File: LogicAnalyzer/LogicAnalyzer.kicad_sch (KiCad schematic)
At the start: 29 parts, among them J1 Conn_02x03_Odd_Even, J2 Connector, J3 Chain, U1 TXB0104PW, U2 TXB0104PW, U3 TXB0104PW, U4 TXB0104PW, U5 TXB0104PW, U6 TXB0104PW, U7 Pico

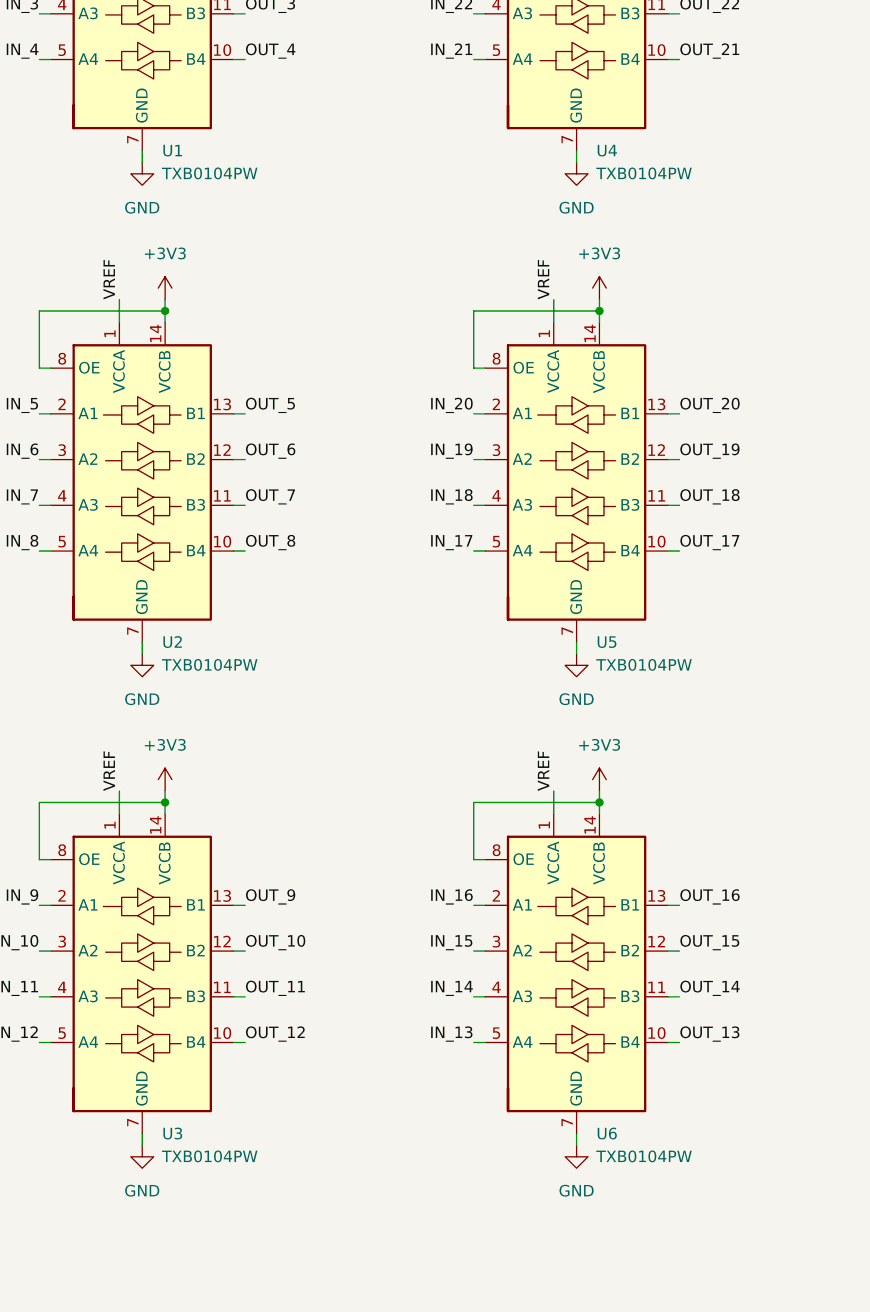
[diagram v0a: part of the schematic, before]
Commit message: Schematic Update Level Shifter Type
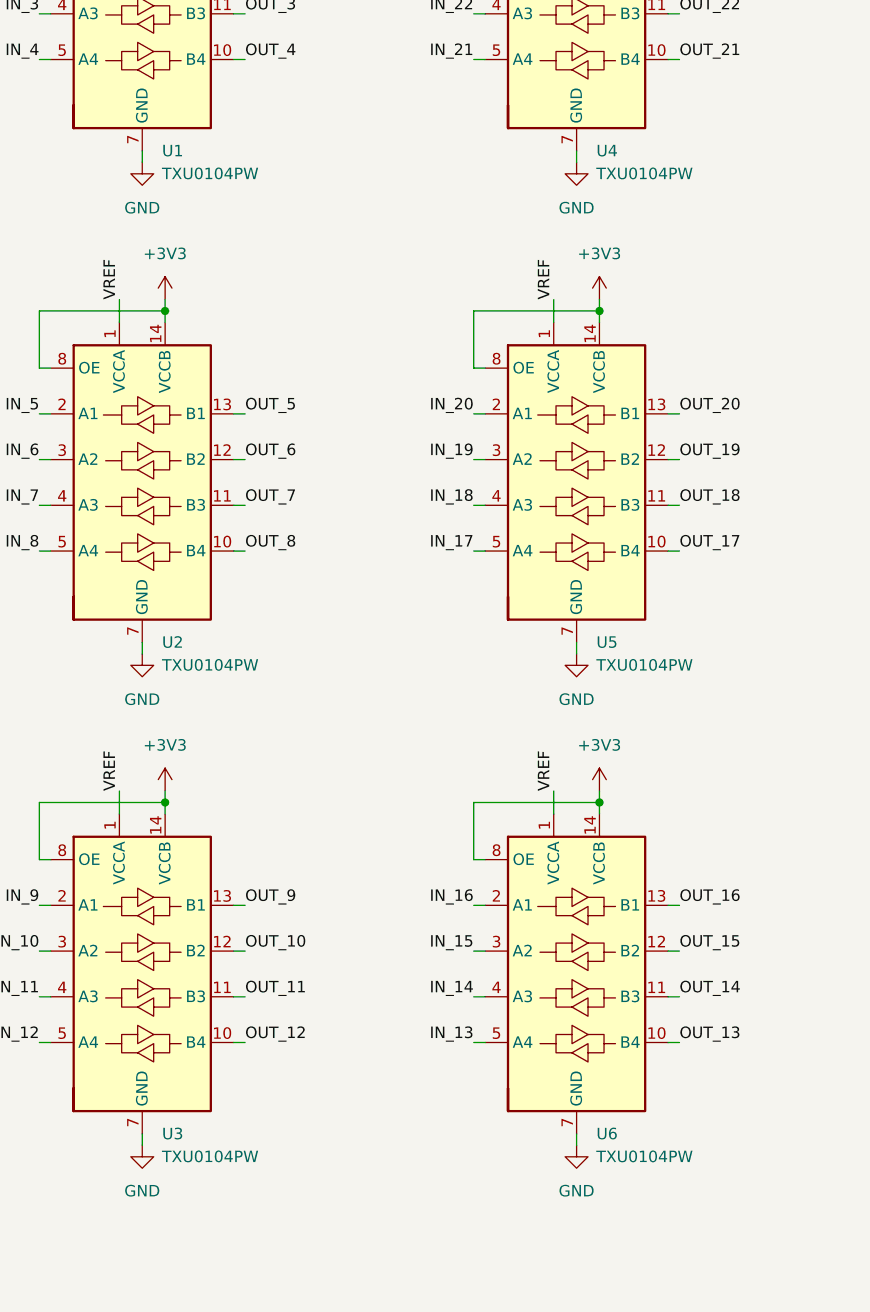
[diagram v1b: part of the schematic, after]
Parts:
- U1, U2, U3, U4, U5, U6: value TXB0104PW -> TXU0104PW
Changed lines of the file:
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@@
 			)
 		)
-		(property "Value" "TXB0104PW"
+		(property "Value" "TXU0104PW"
 			(at 41.5641 181.61 0)
 			(effects
@@
 			)
 		)
-		(property "Datasheet" "http://www.ti.com/lit/ds/symlink/txb0104.pdf"
+		(property "Datasheet" "https://www.ti.com/lit/ds/symlink/txu0104.pdf"
 			(at 42.164 158.877 0)
 			(effects
@@
 			)
 		)
-		(property "Value" "TXB0104PW"
+		(property "Value" "TXU0104PW"
 			(at 89.8241 127 0)
 			(effects
@@
 			)
 		)
-		(property "Datasheet" "http://www.ti.com/lit/ds/symlink/txb0104.pdf"
+		(property "Datasheet" "https://www.ti.com/lit/ds/symlink/txu0104.pdf"
 			(at 90.424 104.267 0)
 			(effects
@@
 			)
 		)
-		(property "Value" "TXB0104PW"
+		(property "Value" "TXU0104PW"
 			(at 89.8241 181.61 0)
 			(effects
@@
 			)
 		)
-		(property "Datasheet" "http://www.ti.com/lit/ds/symlink/txb0104.pdf"
+		(property "Datasheet" "https://www.ti.com/lit/ds/symlink/txu0104.pdf"
 			(at 90.424 158.877 0)
 			(effects
@@
 			)
 		)
-		(property "Value" "TXB0104PW"
+		(property "Value" "TXU0104PW"
 			(at 89.8241 72.39 0)
 			(effects
@@
 			)
 		)
-		(property "Datasheet" "http://www.ti.com/lit/ds/symlink/txb0104.pdf"
+		(property "Datasheet" "https://www.ti.com/lit/ds/symlink/txu0104.pdf"
 			(at 90.424 49.657 0)
 			(effects
@@
 			)
 		)
-		(property "Value" "TXB0104PW"
+		(property "Value" "TXU0104PW"
 			(at 41.5641 127 0)
 			(effects
@@
 			)
 		)
-		(property "Datasheet" "http://www.ti.com/lit/ds/symlink/txb0104.pdf"
+		(property "Datasheet" "https://www.ti.com/lit/ds/symlink/txu0104.pdf"
 			(at 42.164 104.267 0)
 			(effects
@@
 			)
 		)
-		(property "Value" "TXB0104PW"
+		(property "Value" "TXU0104PW"
 			(at 41.5641 72.39 0)
 			(effects
@@
 			)
 		)
-		(property "Datasheet" "http://www.ti.com/lit/ds/symlink/txb0104.pdf"
+		(property "Datasheet" "https://www.ti.com/lit/ds/symlink/txu0104.pdf"
 			(at 42.164 49.657 0)
 			(effects

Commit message: DRC Check
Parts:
- removed H4: MountingHole, MountingHole:MountingHole_3.2mm_M3_DIN965, symbol Mechanical:MountingHole
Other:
- moved on the sheet: H1, H2, H3
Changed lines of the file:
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@@
 	)
 	(symbol
-		(lib_id "Mechanical:MountingHole")
-		(at 132.08 186.69 0)
-		(unit 1)
-		(exclude_from_sim yes)
-		(in_bom no)
-		(on_board yes)
-		(dnp no)
-		(fields_autoplaced yes)
-		(property "Reference" "H4"
-			(at 134.62 185.4199 0)
-			(effects
-				(font
-					(size 1.27 1.27)
-				)
-				(justify left)
-			)
-		)
-		(property "Value" "MountingHole"
-			(at 134.62 187.9599 0)
-			(effects
-				(font
-					(size 1.27 1.27)
-				)
-				(justify left)
-			)
-		)
-		(property "Footprint" "MountingHole:MountingHole_3.2mm_M3_DIN965"
-			(at 132.08 186.69 0)
-			(effects
-				(font
-					(size 1.27 1.27)
-				)
-				(hide yes)
-			)
-		)
-		(property "Datasheet" "~"
-			(at 132.08 186.69 0)
-			(effects
-				(font
-					(size 1.27 1.27)
-				)
-				(hide yes)
-			)
-		)
-		(property "Description" "Mounting Hole without connection"
-			(at 132.08 186.69 0)
-			(effects
-				(font
-					(size 1.27 1.27)
-				)
-				(hide yes)
-			)
-		)
-		(instances
-			(project "LogicAnalyzer"
-				(path "/182dbd66-1aac-4aeb-9621-9909e037a8f2"
-					(reference "H4")
-					(unit 1)
-				)
-			)
-		)
-	)
-	(symbol
 		(lib_id "power:+3V3")
 		(at 261.62 35.56 270)
@@
 	(symbol
 		(lib_id "Mechanical:MountingHole")
-		(at 132.08 171.45 0)
+		(at 140.97 179.07 0)
 		(unit 1)
 		(exclude_from_sim yes)
@@
 		(fields_autoplaced yes)
 		(property "Reference" "H1"
-			(at 134.62 170.1799 0)
+			(at 143.51 177.7999 0)
 			(effects
 				(font
@@
 		)
 		(property "Value" "MountingHole"
-			(at 134.62 172.7199 0)
+			(at 143.51 180.3399 0)
 			(effects
 				(font
@@
 		)
 		(property "Footprint" "MountingHole:MountingHole_3.2mm_M3_DIN965"
-			(at 132.08 171.45 0)
+			(at 140.97 179.07 0)
 			(effects
 				(font
@@
 		)
 		(property "Datasheet" "~"
-			(at 132.08 171.45 0)
+			(at 140.97 179.07 0)
 			(effects
 				(font
@@
 		)
 		(property "Description" "Mounting Hole without connection"
-			(at 132.08 171.45 0)
+			(at 140.97 179.07 0)
 			(effects
 				(font
@@
 	(symbol
 		(lib_id "Mechanical:MountingHole")
-		(at 132.08 181.61 0)
+		(at 140.97 189.23 0)
 		(unit 1)
 		(exclude_from_sim yes)
@@
 		(fields_autoplaced yes)
 		(property "Reference" "H3"
-			(at 134.62 180.3399 0)
+			(at 143.51 187.9599 0)
 			(effects
 				(font
@@
 		)
 		(property "Value" "MountingHole"
-			(at 134.62 182.8799 0)
+			(at 143.51 190.4999 0)
 			(effects
 				(font
@@
 		)
 		(property "Footprint" "MountingHole:MountingHole_3.2mm_M3_DIN965"
-			(at 132.08 181.61 0)
+			(at 140.97 189.23 0)
 			(effects
 				(font
@@
 		)
 		(property "Datasheet" "~"
-			(at 132.08 181.61 0)
+			(at 140.97 189.23 0)
 			(effects
 				(font
@@
 		)
 		(property "Description" "Mounting Hole without connection"
-			(at 132.08 181.61 0)
+			(at 140.97 189.23 0)
 			(effects
 				(font
@@
 	(symbol
 		(lib_id "Mechanical:MountingHole")
-		(at 132.08 176.53 0)
+		(at 140.97 184.15 0)
 		(unit 1)
 		(exclude_from_sim yes)
@@
 		(fields_autoplaced yes)
 		(property "Reference" "H2"
-			(at 134.62 175.2599 0)
+			(at 143.51 182.8799 0)
 			(effects
 				(font
@@
 		)
 		(property "Value" "MountingHole"
-			(at 134.62 177.7999 0)
+			(at 143.51 185.4199 0)
 			(effects
 				(font
@@
 		)
 		(property "Footprint" "MountingHole:MountingHole_3.2mm_M3_DIN965"
-			(at 132.08 176.53 0)
+			(at 140.97 184.15 0)
 			(effects
 				(font
@@
 		)
 		(property "Datasheet" "~"
-			(at 132.08 176.53 0)
+			(at 140.97 184.15 0)
 			(effects
 				(font
@@
 		)
 		(property "Description" "Mounting Hole without connection"
-			(at 132.08 176.53 0)
+			(at 140.97 184.15 0)
 			(effects
 				(font
